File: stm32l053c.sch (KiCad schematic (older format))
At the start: 17 parts, among them P1 SWD, P2 CONN_01X17, P3 CONN_01X17, P4 Ext Xtal, SW1 RESET, U1 STM32L053C8_LQFP48

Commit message: Solder bridges
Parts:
- R2, R3: footprint Resistors_SMD:R_0805_HandSoldering -> Resistors_SMD:R_0402
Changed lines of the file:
@@
 F 0 "R2" V 7180 1450 50  0000 C CNN
 F 1 "0" V 7100 1450 50  0000 C CNN
-F 2 "Resistors_SMD:R_0805_HandSoldering" V 7030 1450 50  0001 C CNN
+F 2 "Resistors_SMD:R_0402" V 7030 1450 50  0001 C CNN
 F 3 "" H 7100 1450 50  0000 C CNN
 	1    7100 1450
@@
 F 0 "R3" V 7880 1450 50  0000 C CNN
 F 1 "0" V 7800 1450 50  0000 C CNN
-F 2 "Resistors_SMD:R_0805_HandSoldering" V 7730 1450 50  0001 C CNN
+F 2 "Resistors_SMD:R_0402" V 7730 1450 50  0001 C CNN
 F 3 "" H 7800 1450 50  0000 C CNN
 	1    7800 1450

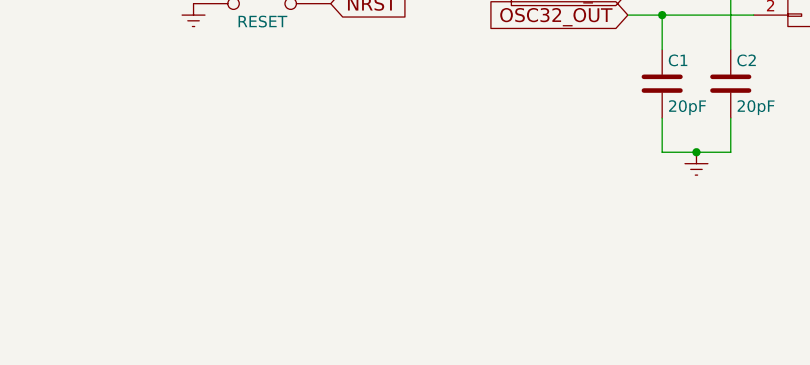
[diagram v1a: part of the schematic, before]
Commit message: LED on "D13"
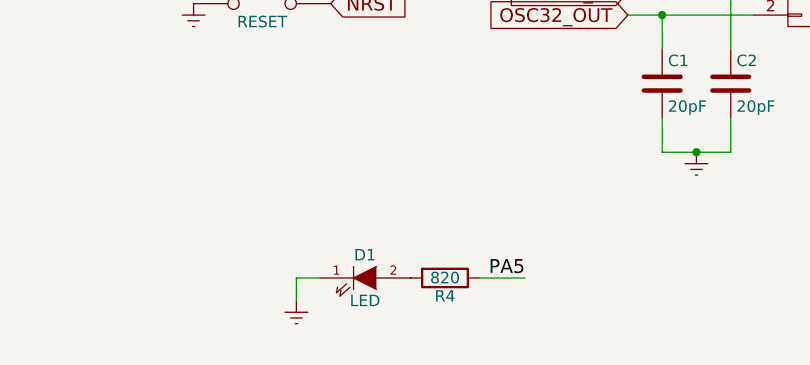
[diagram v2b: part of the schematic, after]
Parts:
- added D1: LED, LEDs:LED_0805, symbol LED
- added R4: 820, Resistors_SMD:R_0805_HandSoldering, symbol R
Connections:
- net Earth: now also D1.1 (K)
- net PA5: now also R4.1
- new net: D1.2 (A), R4.2
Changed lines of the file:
@@
 $EndDescr
 $Comp
-L Earth #PWR01
+L Earth #PWR17
 U 1 1 58021BE1
 P 9650 1350
-F 0 "#PWR01" H 9650 1100 50  0001 C CNN
+F 0 "#PWR17" H 9650 1100 50  0001 C CNN
 F 1 "Earth" H 9650 1200 50  0001 C CNN
 F 2 "" H 9650 1350 50  0000 C CNN
@@
 $EndComp
 $Comp
-L VDD #PWR02
+L VDD #PWR16
 U 1 1 58021C2A
 P 9650 1050
-F 0 "#PWR02" H 9650 900 50  0001 C CNN
+F 0 "#PWR16" H 9650 900 50  0001 C CNN
 F 1 "VDD" H 9650 1200 50  0000 C CNN
 F 2 "" H 9650 1050 50  0000 C CNN
@@
 $EndComp
 $Comp
-L GNDA #PWR03
+L GNDA #PWR12
 U 1 1 58021F75
 P 7050 6200
-F 0 "#PWR03" H 7050 5950 50  0001 C CNN
+F 0 "#PWR12" H 7050 5950 50  0001 C CNN
 F 1 "GNDA" H 7050 6050 50  0000 C CNN
 F 2 "" H 7050 6200 50  0000 C CNN
@@
 $EndComp
 $Comp
-L Earth #PWR04
+L Earth #PWR15
 U 1 1 58021F89
 P 7550 6200
-F 0 "#PWR04" H 7550 5950 50  0001 C CNN
+F 0 "#PWR15" H 7550 5950 50  0001 C CNN
 F 1 "Earth" H 7550 6050 50  0001 C CNN
 F 2 "" H 7550 6200 50  0000 C CNN
@@
 $EndComp
 $Comp
-L GNDA #PWR05
+L GNDA #PWR11
 U 1 1 58022154
 P 7050 5700
-F 0 "#PWR05" H 7050 5450 50  0001 C CNN
+F 0 "#PWR11" H 7050 5450 50  0001 C CNN
 F 1 "GNDA" H 7050 5550 50  0000 C CNN
 F 2 "" H 7050 5700 50  0000 C CNN
@@
 $EndComp
 $Comp
-L Earth #PWR06
+L Earth #PWR14
 U 1 1 580221FA
 P 7550 5700
-F 0 "#PWR06" H 7550 5450 50  0001 C CNN
+F 0 "#PWR14" H 7550 5450 50  0001 C CNN
 F 1 "Earth" H 7550 5550 50  0001 C CNN
 F 2 "" H 7550 5700 50  0000 C CNN
@@
 $EndComp
 $Comp
-L VDD #PWR07
+L VDD #PWR13
 U 1 1 5802295B
 P 7350 950
-F 0 "#PWR07" H 7350 800 50  0001 C CNN
+F 0 "#PWR13" H 7350 800 50  0001 C CNN
 F 1 "VDD" H 7350 1100 50  0000 C CNN
 F 2 "" H 7350 950 50  0000 C CNN
@@
 $EndComp
 $Comp
-L Earth #PWR08
+L Earth #PWR10
 U 1 1 5803310F
 P 6700 1700
-F 0 "#PWR08" H 6700 1450 50  0001 C CNN
+F 0 "#PWR10" H 6700 1450 50  0001 C CNN
 F 1 "Earth" H 6700 1550 50  0001 C CNN
 F 2 "" H 6700 1700 50  0000 C CNN
@@
 $EndComp
 $Comp
-L Earth #PWR09
+L Earth #PWR9
 U 1 1 58034EA2
 P 5800 5450
-F 0 "#PWR09" H 5800 5200 50  0001 C CNN
+F 0 "#PWR9" H 5800 5200 50  0001 C CNN
 F 1 "Earth" H 5800 5300 50  0001 C CNN
 F 2 "" H 5800 5450 50  0000 C CNN
@@
 $EndComp
 $Comp
-L Earth #PWR010
+L Earth #PWR6
 U 1 1 580369A9
 P 2400 1350
-F 0 "#PWR010" H 2400 1100 50  0001 C CNN
+F 0 "#PWR6" H 2400 1100 50  0001 C CNN
 F 1 "Earth" H 2400 1200 50  0001 C CNN
 F 2 "" H 2400 1350 50  0000 C CNN
@@
 SWO
 $Comp
-L VDD #PWR011
+L VDD #PWR4
 U 1 1 5803734F
 P 1900 1150
-F 0 "#PWR011" H 1900 1000 50  0001 C CNN
+F 0 "#PWR4" H 1900 1000 50  0001 C CNN
 F 1 "VDD" H 1900 1300 50  0000 C CNN
 F 2 "" H 1900 1150 50  0000 C CNN
@@
 PC13
 $Comp
-L VDD #PWR012
+L VDD #PWR2
 U 1 1 5803DE79
 P 1500 2500
-F 0 "#PWR012" H 1500 2350 50  0001 C CNN
+F 0 "#PWR2" H 1500 2350 50  0001 C CNN
 F 1 "VDD" H 1500 2650 50  0000 C CNN
 F 2 "" H 1500 2500 50  0000 C CNN
@@
 $EndComp
 $Comp
-L Earth #PWR013
+L Earth #PWR3
 U 1 1 5803F003
 P 1850 4900
-F 0 "#PWR013" H 1850 4650 50  0001 C CNN
+F 0 "#PWR3" H 1850 4650 50  0001 C CNN
 F 1 "Earth" H 1850 4750 50  0001 C CNN
 F 2 "" H 1850 4900 50  0000 C CNN
@@
 NRST
 $Comp
-L Earth #PWR014
+L Earth #PWR19
 U 1 1 58039244
 P 9650 2100
-F 0 "#PWR014" H 9650 1850 50  0001 C CNN
+F 0 "#PWR19" H 9650 1850 50  0001 C CNN
 F 1 "Earth" H 9650 1950 50  0001 C CNN
 F 2 "" H 9650 2100 50  0000 C CNN
@@
 $EndComp
 $Comp
-L VDD #PWR015
+L VDD #PWR18
 U 1 1 5803924A
 P 9650 1800
-F 0 "#PWR015" H 9650 1650 50  0001 C CNN
+F 0 "#PWR18" H 9650 1650 50  0001 C CNN
 F 1 "VDD" H 9650 1950 50  0000 C CNN
 F 2 "" H 9650 1800 50  0000 C CNN
@@
 $EndComp
 $Comp
-L Earth #PWR016
+L Earth #PWR20
 U 1 1 5803BDC8
 P 10700 1350
-F 0 "#PWR016" H 10700 1100 50  0001 C CNN
+F 0 "#PWR20" H 10700 1100 50  0001 C CNN
 F 1 "Earth" H 10700 1200 50  0001 C CNN
 F 2 "" H 10700 1350 50  0000 C CNN
@@
 VDDA
 $Comp
-L Earth #PWR017
+L Earth #PWR1
 U 1 1 5803D0EB
 P 750 2650
-F 0 "#PWR017" H 750 2400 50  0001 C CNN
+F 0 "#PWR1" H 750 2400 50  0001 C CNN
 F 1 "Earth" H 750 2500 50  0001 C CNN
 F 2 "" H 750 2650 50  0000 C CNN
@@
 $EndComp
 $Comp
-L Earth #PWR018
+L Earth #PWR7
 U 1 1 58065816
 P 2650 3000
-F 0 "#PWR018" H 2650 2750 50  0001 C CNN
+F 0 "#PWR7" H 2650 2750 50  0001 C CNN
 F 1 "Earth" H 2650 2850 50  0001 C CNN
 F 2 "" H 2650 3000 50  0000 C CNN
@@
 Connection ~ 4200 4850
 $Comp
-L Earth #PWR019
+L Earth #PWR8
 U 1 1 5806680D
 P 4050 5550
-F 0 "#PWR019" H 4050 5300 50  0001 C CNN
+F 0 "#PWR8" H 4050 5300 50  0001 C CNN
 F 1 "Earth" H 4050 5400 50  0001 C CNN
 F 2 "" H 4050 5550 50  0000 C CNN
@@
 Text Label 5800 5000 0    60   ~ 0
 OSC_OUT
+$Comp
+L LED D1
+U 1 1 58076AE7
+P 2600 6100
+F 0 "D1" H 2600 6200 50  0000 C CNN
+F 1 "LED" H 2600 6000 50  0000 C CNN
+F 2 "LEDs:LED_0805" H 2600 6100 50  0001 C CNN
+F 3 "" H 2600 6100 50  0000 C CNN
+	1    2600 6100
+	1    0    0    -1
+$EndComp
+$Comp
+L R R4
+U 1 1 580770D7
+P 2950 6100
+F 0 "R4" V 3030 6100 50  0000 C CNN
+F 1 "820" V 2950 6100 50  0000 C CNN
+F 2 "Resistors_SMD:R_0805_HandSoldering" V 2880 6100 50  0001 C CNN
+F 3 "" H 2950 6100 50  0000 C CNN
+	1    2950 6100
+	0    1    1    0
+$EndComp
+$Comp
+L Earth #PWR5
+U 1 1 58077163
+P 2300 6200
+F 0 "#PWR5" H 2300 5950 50  0001 C CNN
+F 1 "Earth" H 2300 6050 50  0001 C CNN
+F 2 "" H 2300 6200 50  0000 C CNN
+F 3 "" H 2300 6200 50  0000 C CNN
+	1    2300 6200
+	1    0    0    -1
+$EndComp
+Wire Wire Line
+	2300 6200 2300 6100
+Wire Wire Line
+	2300 6100 2400 6100
+Text Label 3300 6100 2    60   ~ 0
+PA5
+Wire Wire Line
+	3300 6100 3100 6100
 $EndSCHEMATC
